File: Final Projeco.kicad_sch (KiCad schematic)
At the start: 28 parts, among them U1 ESP32-S3, U2 GT-USB-7004N, U3 NCP167BMX330TBG, U4 LY68L6400SLIT, U5 PTS830GG140SMTRLFS, U6 PTS830GG140SMTRLFS, U7 220S-2*16P_H=8_5MM_Ytype_L=3_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, X1 TZ1269D

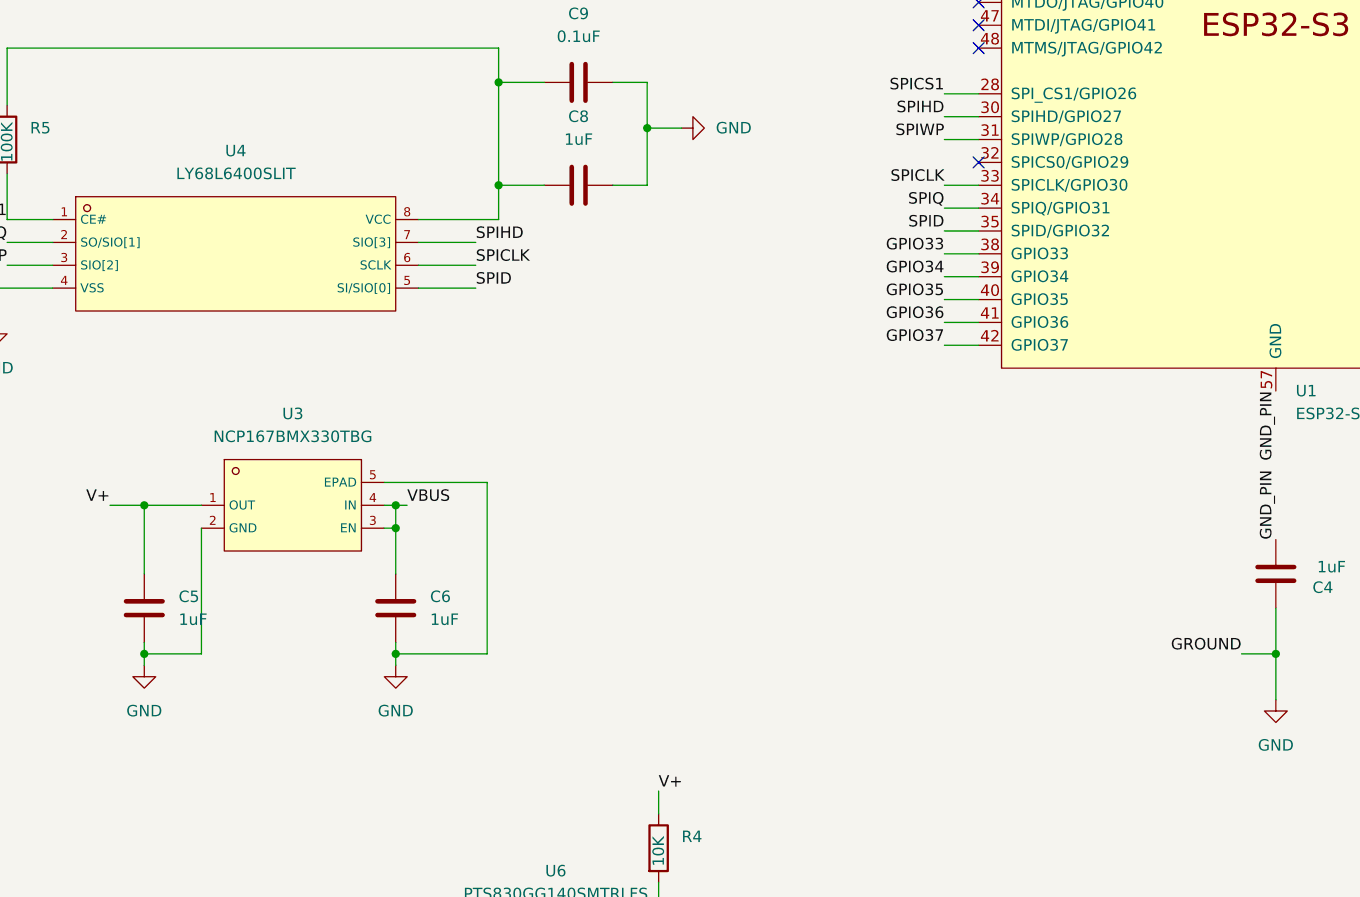
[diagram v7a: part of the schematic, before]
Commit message: -Final Draft Submission mk2
-Added bypass caps across 3.3 & GND to make signal less ripple-y
-added component to replace SRAM chip:
https://jlcpcb.com/partdetail/Zetta-ZD25Q32CTIGT/C3029778
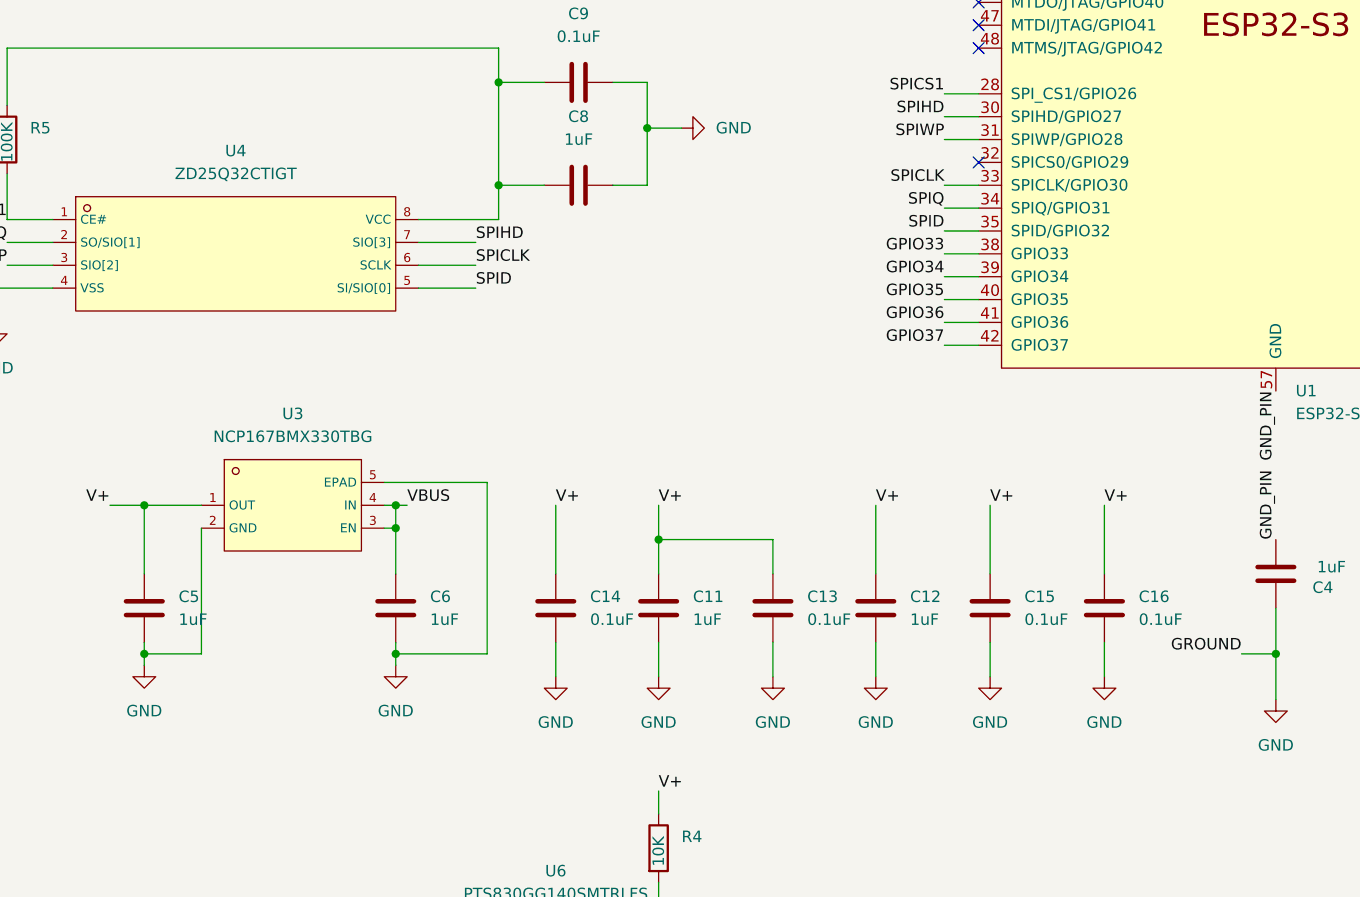
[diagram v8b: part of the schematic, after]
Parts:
- added C11, C12: 1uF, Capacitor_SMD:C_0402_1005Metric, symbol Device:C
- added C13, C14, C15, C16: 0.1uF, Capacitor_SMD:C_0402_1005Metric, symbol Device:C
- U4: value LY68L6400SLIT -> ZD25Q32CTIGT
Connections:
- net GND: now also C11.2, C12.2, C13.1, C14.1, C15.1, C16.1
- net VDD3P3: now also C11.1, C12.1, C13.2, C14.2, C15.2, C16.2
